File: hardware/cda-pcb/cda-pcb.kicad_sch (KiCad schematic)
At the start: 187 parts, among them J1 ICD15S13E4GX00LF, J2 ICD15S13E4GX00LF, J3 ICD15S13E4GX00LF, J4 ICD15S13E4GX00LF, J6 Conn_01x06, P1 0022272021, U1 ADS124S08IRHBT, U10 SN74AHCT125RGYR, U2 ADS124S08IRHBT, U3 ADS124S08IRHBT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

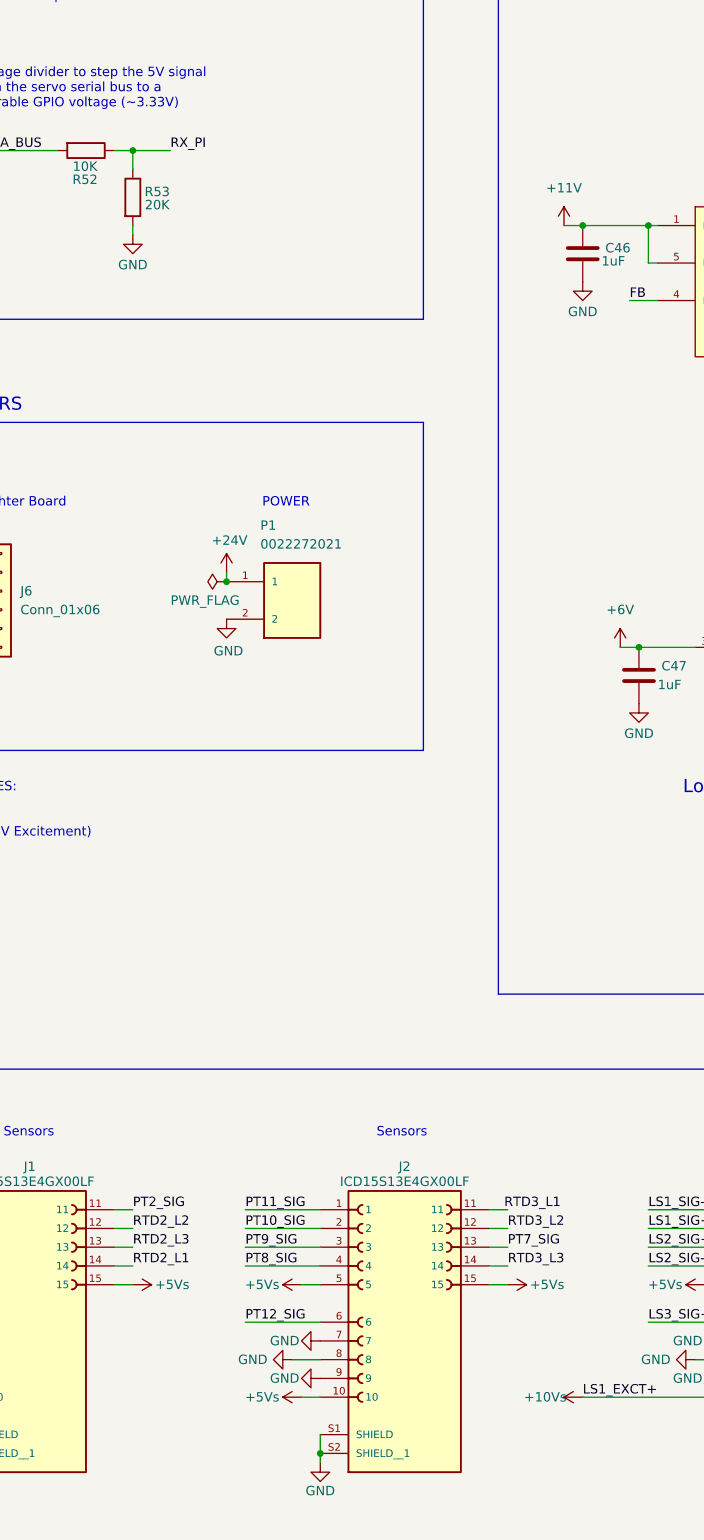
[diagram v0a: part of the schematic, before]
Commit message: change name to cda-pcb (control and data acquisition)
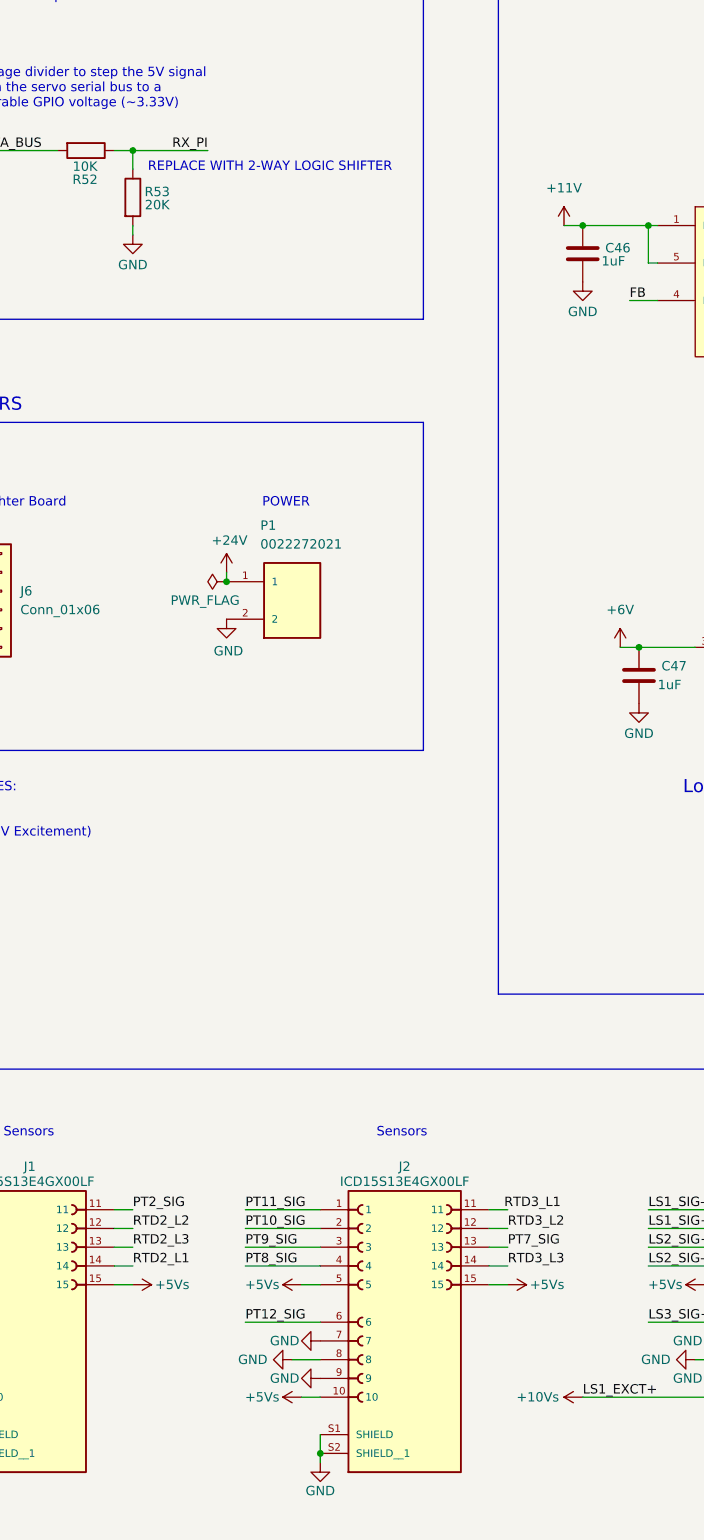
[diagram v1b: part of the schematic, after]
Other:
- note added: "REPLACE WITH 2-WAY LOGIC SHIFTER"
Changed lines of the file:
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@@
 		)
 	)
+	(text "REPLACE WITH 2-WAY LOGIC SHIFTER"
+		(exclude_from_sim no)
+		(at 296.672 202.946 0)
+		(effects
+			(font
+				(size 1.27 1.27)
+			)
+			(justify left)
+		)
+	)
 	(text "INPUT ESD and SURGE PROTECTION"
 		(exclude_from_sim no)
@@
 	(wire
 		(pts
-			(xy 294.64 200.66) (xy 299.72 200.66)
+			(xy 294.64 200.66) (xy 304.8 200.66)
 		)
 		(stroke
@@
 	)
 	(label "RX_PI"
-		(at 299.72 200.66 0)
+		(at 304.8 200.66 180)
 		(effects
 			(font
 				(size 1.27 1.27)
 			)
-			(justify left bottom)
+			(justify right bottom)
 		)
 	)
@@
 		)
 		(property "Value" "+10Vs"
-			(at 350.52 369.57 90)
+			(at 349.504 369.57 90)
 			(effects
 				(font

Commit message: EVERYTHING IS ROUTED RRAHHHH
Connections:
- net +10Vs: now also D11.3 (K_2); no longer D11.1 (K_1)
- net IDAC2_1: now also D6.1, J3.13; no longer J3.14
- net LS1_SIG-: now also D8.1; no longer D7.1
- net LS2_SIG+: now also D7.1, J3.4; no longer D7.3, J3.3
- net LS2_SIG-: now also D7.3, J3.3; no longer D8.1, J3.4
- net RTD1_L1: now also D6.6, J3.14; no longer J3.12
- net RTD1_L3: now also D8.6, J3.12; no longer J3.13
- no-connect marks 31 -> 30
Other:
- note removed: "REPLACE WITH 2-WAY LOGIC SHIFTER"
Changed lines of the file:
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@@
 		)
 	)
-	(text "REPLACE WITH 2-WAY LOGIC SHIFTER"
-		(exclude_from_sim no)
-		(at 296.672 202.946 0)
-		(effects
-			(font
-				(size 1.27 1.27)
-			)
-			(justify left)
-		)
-	)
 	(text "INPUT ESD and SURGE PROTECTION"
 		(exclude_from_sim no)
@@
 	)
 	(no_connect
+		(at 318.77 115.57)
+	)
+	(no_connect
 		(at 534.67 59.69)
 	)
@@
 	)
 	(no_connect
-		(at 318.77 120.65)
-	)
-	(no_connect
 		(at 210.82 55.88)
 	)
@@
 	)
 	(no_connect
-		(at 346.71 90.17)
-	)
-	(no_connect
 		(at 523.24 182.88)
 	)
@@
 	(wire
 		(pts
+			(xy 308.61 120.65) (xy 318.77 120.65)
+		)
+		(stroke
+			(width 0)
+			(type default)
+		)
+	)
+	(wire
+		(pts
 			(xy 487.68 157.48) (xy 487.68 165.1)
 		)
@@
 	(wire
 		(pts
-			(xy 309.88 118.11) (xy 318.77 118.11)
+			(xy 308.61 118.11) (xy 318.77 118.11)
 		)
 		(stroke
@@
 	(wire
 		(pts
-			(xy 309.88 115.57) (xy 318.77 115.57)
-		)
-		(stroke
-			(width 0)
-			(type default)
-		)
-	)
-	(wire
-		(pts
 			(xy 140.97 119.38) (xy 148.59 119.38)
 		)
@@
 	(wire
 		(pts
-			(xy 346.71 100.33) (xy 344.17 100.33)
+			(xy 354.33 100.33) (xy 344.17 100.33)
 		)
 		(stroke
@@
 	(wire
 		(pts
-			(xy 346.71 90.17) (xy 344.17 90.17)
+			(xy 353.06 90.17) (xy 344.17 90.17)
 		)
 		(stroke
@@
 		)
 	)
-	(label "LS2_SIG+"
-		(at 256.54 100.33 0)
-		(effects
-			(font
-				(size 1.27 1.27)
-			)
-			(justify left bottom)
-		)
-	)
 	(label "OTVV"
 		(at 447.04 74.93 0)
@@
 		)
 	)
-	(label "LS1_EXCT+"
-		(at 309.88 115.57 0)
-		(effects
-			(font
-				(size 1.27 1.27)
-			)
-			(justify left bottom)
-		)
-	)
 	(label "OMV"
 		(at 447.04 59.69 0)
@@
 		)
 	)
+	(label "LS2_SIG+"
+		(at 256.54 90.17 0)
+		(effects
+			(font
+				(size 1.27 1.27)
+			)
+			(justify left bottom)
+		)
+	)
 	(label "POFFV"
 		(at 416.56 354.33 0)
@@
 		)
 	)
-	(label "LS2_SIG+"
-		(at 364.49 349.25 0)
-		(effects
-			(font
-				(size 1.27 1.27)
-			)
-			(justify left bottom)
-		)
-	)
 	(label "RTD2_L3"
 		(at 256.54 54.61 0)
@@
 		)
 	)
+	(label "LS1_EXCT+"
+		(at 308.61 120.65 0)
+		(effects
+			(font
+				(size 1.27 1.27)
+			)
+			(justify left bottom)
+		)
+	)
 	(label "OFFV"
 		(at 256.54 113.03 0)
@@
 	)
 	(label "RTD1_L1"
-		(at 243.84 59.69 0)
+		(at 406.4 67.31 180)
 		(effects
 			(font
 				(size 1.27 1.27)
 			)
-			(justify left bottom)
+			(justify right bottom)
 		)
 	)
@@
 	)
 	(label "RTD1_L3"
-		(at 243.84 64.77 0)
+		(at 353.06 90.17 180)
 		(effects
 			(font
 				(size 1.27 1.27)
 			)
-			(justify left bottom)
+			(justify right bottom)
 		)
 	)
@@
 		)
 	)
-	(label "PT11_SIG"
-		(at 353.06 77.47 180)
+	(label "RTD1_L2"
+		(at 400.05 349.25 0)
 		(effects
 			(font
 				(size 1.27 1.27)
 			)
-			(justify right bottom)
+			(justify left bottom)
 		)
 	)
-	(label "RTD1_L1"
-		(at 400.05 346.71 0)
+	(label "PT11_SIG"
+		(at 353.06 77.47 180)
 		(effects
 			(font
 				(size 1.27 1.27)
 			)
-			(justify left bottom)
+			(justify right bottom)
 		)
 	)
@@
 		)
 	)
-	(label "LS2_SIG-"
-		(at 308.61 90.17 0)
+	(label "RTD1_L2"
+		(at 361.95 67.31 0)
 		(effects
 			(font
@@
 		)
 	)
-	(label "RTD1_L2"
-		(at 400.05 351.79 0)
-		(effects
-			(font
-				(size 1.27 1.27)
-			)
-			(justify left bottom)
-		)
-	)
 	(label "DATA_BUS"
 		(at 273.05 200.66 0)
@@
 		)
 	)
+	(label "LS2_SIG+"
+		(at 364.49 351.79 0)
+		(effects
+			(font
+				(size 1.27 1.27)
+			)
+			(justify left bottom)
+		)
+	)
 	(label "OIMV{slash}FIMV{slash}SPARK"
 		(at 441.96 80.01 0)
@@
 		)
 	)
+	(label "LS1_SIG-"
+		(at 308.61 90.17 0)
+		(effects
+			(font
+				(size 1.27 1.27)
+			)
+			(justify left bottom)
+		)
+	)
 	(label "DRDY_N2"
 		(at 218.44 187.96 0)
@@
 		)
 	)
-	(label "RTD1_L2"
-		(at 243.84 54.61 0)
-		(effects
-			(font
-				(size 1.27 1.27)
-			)
-			(justify left bottom)
-		)
-	)
 	(label "TX_ENABLE"
 		(at 260.35 151.13 0)
@@
 		)
 	)
-	(label "LS1_SIG-"
-		(at 256.54 90.17 0)
+	(label "RTD2_L2"
+		(at 294.64 346.71 0)
 		(effects
 			(font
@@
 	)
 	(label "RTD2_L2"
-		(at 294.64 346.71 0)
+		(at 256.54 44.45 0)
 		(effects
 			(font
@@
 		)
 	)
-	(label "RTD2_L2"
-		(at 256.54 44.45 0)
+	(label "LS3_SIG-"
+		(at 354.33 100.33 180)
 		(effects
 			(font
 				(size 1.27 1.27)
 			)
-			(justify left bottom)
+			(justify right bottom)
 		)
 	)
-	(label "LS3_SIG-"
-		(at 346.71 100.33 0)
+	(label "DRDY_N3"
+		(at 544.83 69.85 0)
 		(effects
 			(font
@@
 		)
 	)
-	(label "DRDY_N3"
-		(at 544.83 69.85 0)
+	(label "RTD1_L3"
+		(at 400.05 346.71 0)
 		(effects
 			(font
@@
 		)
 	)
-	(label "RTD1_L3"
-		(at 400.05 349.25 0)
-		(effects
-			(font
-				(size 1.27 1.27)
-			)
-			(justify left bottom)
-		)
-	)
-	(label "LS2_SIG-"
-		(at 364.49 351.79 0)
-		(effects
-			(font
-				(size 1.27 1.27)
-			)
-			(justify left bottom)
-		)
-	)
 	(label "LS3_SIG+"
 		(at 364.49 359.41 0)
@@
 		)
 	)
+	(label "RTD1_L1"
+		(at 400.05 351.79 0)
+		(effects
+			(font
+				(size 1.27 1.27)
+			)
+			(justify left bottom)
+		)
+	)
+	(label "LS2_SIG-"
+		(at 256.54 100.33 0)
+		(effects
+			(font
+				(size 1.27 1.27)
+			)
+			(justify left bottom)
+		)
+	)
 	(label "PT9_SIG"
 		(at 309.88 67.31 0)
@@
 		)
 	)
+	(label "LS2_SIG-"
+		(at 364.49 349.25 0)
+		(effects
+			(font
+				(size 1.27 1.27)
+			)
+			(justify left bottom)
+		)
+	)
 	(label "FTVV"
 		(at 414.02 369.57 0)
@@
 	(symbol
 		(lib_id "power:GND")
-		(at 309.88 118.11 270)
+		(at 308.61 118.11 270)
 		(unit 1)
 		(exclude_from_sim no)
@@
 		(dnp no)
 		(property "Reference" "#PWR081"
-			(at 303.53 118.11 0)
+			(at 302.26 118.11 0)
 			(effects
 				(font
@@
 		)
 		(property "Value" "GND"
-			(at 306.324 118.11 0)
+			(at 305.054 118.11 0)
 			(effects
 				(font
@@
 		)
 		(property "Footprint" ""
-			(at 309.88 118.11 0)
+			(at 308.61 118.11 0)
 			(effects
 				(font
@@
 		)
 		(property "Datasheet" ""
-			(at 309.88 118.11 0)
+			(at 308.61 118.11 0)
 			(effects
 				(font
@@
 		)
 		(property "Description" "Power symbol creates a global label with name \"GND\" , ground"
-			(at 309.88 118.11 0)
+			(at 308.61 118.11 0)
 			(effects
 				(font

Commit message: ERC complete
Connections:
- net GND: now also U10.15 (EPAD)
- no-connect marks 30 -> 31
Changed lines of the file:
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@@
 	)
 	(no_connect
+		(at 400.05 54.61)
+	)
+	(no_connect
 		(at 358.14 168.91)
 	)
@@
 	)
 	(no_connect
+		(at 400.05 77.47)
+	)
+	(no_connect
 		(at 416.56 359.41)
 	)
@@
 	)
 	(no_connect
-		(at 313.69 151.13)
-	)
-	(no_connect
 		(at 154.94 213.36)
 	)
@@
 	(wire
 		(pts
+			(xy 313.69 147.32) (xy 313.69 151.13)
+		)
+		(stroke
+			(width 0)
+			(type default)
+		)
+	)
+	(wire
+		(pts
 			(xy 302.26 90.17) (xy 292.1 90.17)
 		)
@@
 	(wire
 		(pts
+			(xy 316.23 147.32) (xy 313.69 147.32)
+		)
+		(stroke
+			(width 0)
+			(type default)
+		)
+	)
+	(wire
+		(pts
 			(xy 309.88 359.41) (xy 320.04 359.41)
 		)
@@
 	(wire
 		(pts
-			(xy 320.04 151.13) (xy 320.04 153.67)
+			(xy 320.04 148.59) (xy 320.04 153.67)
 		)
 		(stroke
@@
 	(symbol
 		(lib_id "power:+5V")
-		(at 320.04 151.13 0)
+		(at 320.04 148.59 0)
 		(unit 1)
 		(exclude_from_sim no)
@@
 		(dnp no)
 		(property "Reference" "#PWR0182"
-			(at 320.04 154.94 0)
+			(at 320.04 152.4 0)
 			(effects
 				(font
@@
 		)
 		(property "Value" "+5Vs"
-			(at 320.04 146.812 0)
+			(at 320.04 144.272 0)
 			(effects
 				(font
@@
 		)
 		(property "Footprint" ""
-			(at 320.04 151.13 0)
+			(at 320.04 148.59 0)
 			(effects
 				(font
@@
 		)
 		(property "Datasheet" ""
-			(at 320.04 151.13 0)
+			(at 320.04 148.59 0)
 			(effects
 				(font
@@
 		)
 		(property "Description" "Power symbol creates a global label with name \"+5V\""
-			(at 320.04 151.13 0)
+			(at 320.04 148.59 0)
 			(effects
 				(font
@@
 					(unit 1)
 				)
+			)
+		)
+	)
+	(symbol
+		(lib_id "power:GND")
+		(at 316.23 147.32 0)
+		(unit 1)
+		(exclude_from_sim no)
+		(in_bom yes)
+		(on_board yes)
+		(dnp no)
+		(property "Reference" "#PWR0177"
+			(at 316.23 153.67 0)
+			(effects
+				(font
+					(size 1.27 1.27)
+				)
+				(hide yes)
+			)
+		)
+		(property "Value" "GND"
+			(at 316.23 151.384 0)
+			(effects
+				(font
+					(size 1.27 1.27)
+				)
+			)
+		)
+		(property "Footprint" ""
+			(at 316.23 147.32 0)
+			(effects
+				(font
+					(size 1.27 1.27)
+				)
+				(hide yes)
+			)
+		)
+		(property "Datasheet" ""
+			(at 316.23 147.32 0)
+			(effects
+				(font
+					(size 1.27 1.27)
+				)
+				(hide yes)
+			)
+		)
+		(property "Description" "Power symbol creates a global label with name \"GND\" , ground"
+			(at 316.23 147.32 0)
+			(effects
+				(font
+					(size 1.27 1.27)
+				)
+				(hide yes)
+			)
+		)
+		(pin "1"
+		)
+		(instances
+			(project "cda-pcb"
+				(path "/98ce85a8-ddff-4ecb-9668-dd271ba07a43"
+					(reference "#PWR0177")
+					(unit 1)
+				)
